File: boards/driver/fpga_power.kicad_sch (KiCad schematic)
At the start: 55 parts, among them J2 Barrel_Jack_Switch, J3 Conn_01x24, J4 Conn_01x24, Q87 IRF7413, U10 74LVC245, U11 74LVC245, U12 ADP151-3.3, U13 LTC4231-1, U14 74HC4514, U15 74LVC2G04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

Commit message: Driver: minor schematic cleanup and populated all of the BOM except for resistors
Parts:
- added H10, H9: MountingHole, MountingHole:MountingHole_2mm, symbol Mechanical:MountingHole
- added TP1, TP2, TP3, TP4: TestPoint, TestPoint:TestPoint_Keystone_5000-5004_Miniature, symbol Connector:TestPoint
- C45, C46, C53, C54, C55, C56, C57: MPN (none) -> CL10B104KB8NNWC; Manufacturer (none) -> Samsung Electro-Mechanics; Package (none) -> 0603; Rating (none) -> 50V; Tolerance (none) -> 10%
- C47, C48: MPN (none) -> CL21B105KAFNNNE; Manufacturer (none) -> Samsung Electro-Mechanics; Package (none) -> 0805; Rating (none) -> 25V; Tolerance (none) -> 10%
- C49, C50: MPN (none) -> CL10B105KA8NNNC; Manufacturer (none) -> Samsung Electro-Mechanics; Package (none) -> 0603; Rating (none) -> 25V; Tolerance (none) -> 10%
- C51: MPN (none) -> CL10B101KB8NFNC; Manufacturer (none) -> Samsung Electro-Mechanics; Package (none) -> 0603; Rating (none) -> 50V; Tolerance (none) -> 10%
- C52: MPN (none) -> CL10B103KC8NNNC; Manufacturer (none) -> Samsung Electro-Mechanics; Package (none) -> 0603
- D155: MPN (none) -> SMLD12BN1WT86; Manufacturer (none) -> Rohm Semiconductor; Package (none) -> 0603
- D156: MPN (none) -> SMLD12E3N1WT86; Manufacturer (none) -> Rohm Semiconductor; Package (none) -> 0603
- D157: MPN (none) -> SJW1151CKS-100-TR; Manufacturer (none) -> Stanley Electric Co; Package (none) -> 0603
- H1, H2, H3, H4, H5, H6, H7, H8: MPN (none) -> -
- J2: MPN (none) -> PJ-002A; Manufacturer (none) -> CUI Devices; Package (none) -> TH
- J3, J4: MPN (none) -> PPPC241LFBN-RC; Manufacturer (none) -> Sullins Connector Solutions; Package (none) -> TH
- Q87: MPN (none) -> IRF7413ZTRPBF; Manufacturer (none) -> Infineon Technologies; Package (none) -> 8-SOIC
- U10, U11: MPN (none) -> SN74LVC245APWT; Manufacturer (none) -> Texas Instruments; Package (none) -> 20-TSSOP
- U12: MPN (none) -> ADP151AUJZ-3.3-R7; Manufacturer (none) -> Analog Devices, Inc; Package (none) -> TSOT-23-5
- U13: MPN (none) -> LTC4231CMS-1#PBF; Manufacturer (none) -> Analog Devices, Inc; Package (none) -> 12-TSSOP
- U14: MPN (none) -> CD74HC4514M96; Manufacturer (none) -> Texas Instruments; Package (none) -> 24-SOIC
- U15, U16, U17, U18: MPN (none) -> SN74LVC2G04DBVT; Manufacturer (none) -> Texas Instruments; Package (none) -> SOT-23-6
- U9: MPN (none) -> TEN 5-1221‎; Manufacturer (none) -> Traco Power; Package (none) -> 24-DIP
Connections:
- net +14V: now also TP4.1
- net GND: now also TP1.1, TP2.1, TP3.1
- net +3V3 renamed +3.3V
- no-connect marks 4 -> 9

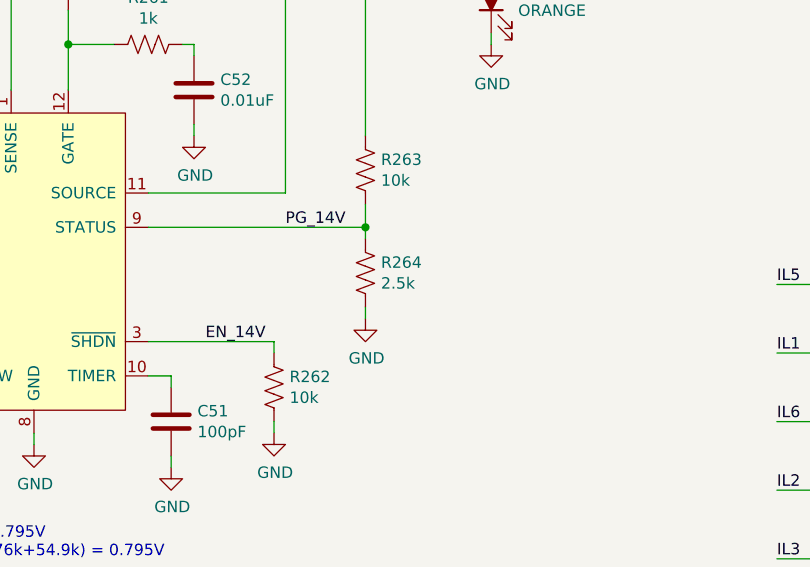
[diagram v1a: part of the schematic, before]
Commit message: Driver: filled out the rest of the BOM, except for defaults for nominal resistances
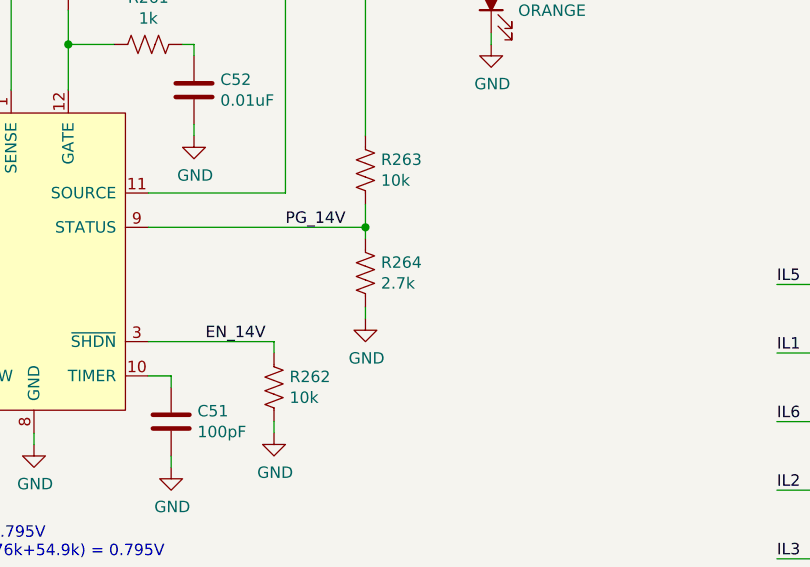
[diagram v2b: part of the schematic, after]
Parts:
- R249, R250: MPN (none) -> RMCF0805ZT0R00; Manufacturer (none) -> Stackpole Electronics Inc; Package (none) -> 0805; Rating (none) -> 1/8W
- R251, R252: MPN (none) -> ERJ-PA3F2001V; Manufacturer (none) -> Panasonic Electronic Components; Package (none) -> 0603; Rating (none) -> 1/3W; Tolerance (none) -> 1%
- R253: MPN (none) -> ERA-3AEB123V; Manufacturer (none) -> Panasonic Electronic Components; Package (none) -> 0603; Rating (none) -> 1/10W; Tolerance (none) -> 0.1%
- R254: MPN (none) -> ERJ-PB3B2401V; Manufacturer (none) -> Panasonic Electronic Components; Package (none) -> 0603; Rating (none) -> 1/5W; Tolerance (none) -> 0.1%
- R255: MPN (none) -> RMCF0603FT1M02; Manufacturer (none) -> Stackpole Electronics Inc; Package (none) -> 0603; Rating (none) -> 1/10W; Tolerance (none) -> 1%
- R256: MPN (none) -> RMCF0603FT2K87; Manufacturer (none) -> Stackpole Electronics Inc; Package (none) -> 0603; Rating (none) -> 1/10W; Tolerance (none) -> 1%
- R257: MPN (none) -> RMCF0603FT9K76; Manufacturer (none) -> Stackpole Electronics Inc; Package (none) -> 0603; Rating (none) -> 1/10W; Tolerance (none) -> 1%
- R258: MPN (none) -> RMCF0603FT54K9; Manufacturer (none) -> Stackpole Electronics Inc; Package (none) -> 0603; Rating (none) -> 1/10W; Tolerance (none) -> 1%
- R259: MPN (none) -> CSR1206FK25L0; Manufacturer (none) -> Stackpole Electronics Inc; Package (none) -> 1206; Rating (none) -> 1/2W; Tolerance (none) -> 1%
- R260: MPN (none) -> ESR03EZPF10R0; Manufacturer (none) -> Rohm Semiconductor; Package (none) -> 0603; Rating (none) -> 1/4W; Tolerance (none) -> 1%
- R261, R265: MPN (none) -> ESR03EZPF1001; Manufacturer (none) -> Rohm Semiconductor; Package (none) -> 0603; Rating (none) -> 1/4W; Tolerance (none) -> 1%
- R262, R263: MPN (none) -> RMCF0603FT10K0; Manufacturer (none) -> Stackpole Electronics Inc; Package (none) -> 0603; Rating (none) -> 1/10W; Tolerance (none) -> 1%
- R264: value 2.5k -> 2.7k; MPN (none) -> RMCF0603JT2K70; Manufacturer (none) -> Stackpole Electronics Inc; Package (none) -> 0603; Rating (none) -> 1/10W; Tolerance (none) -> 1%

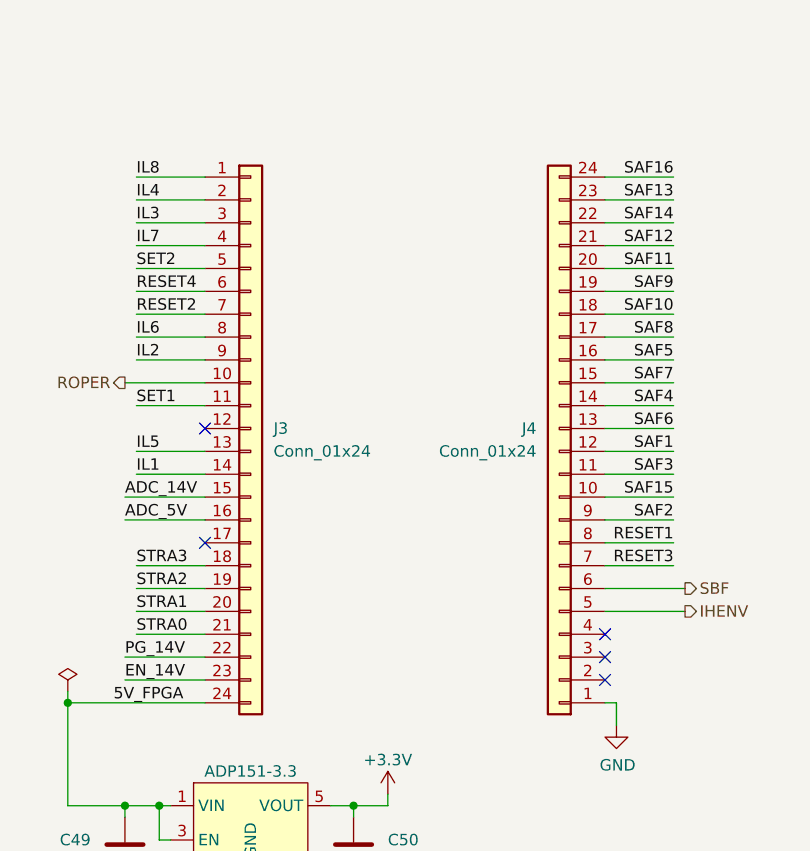
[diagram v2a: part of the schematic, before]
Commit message: Driver: added FPGA ball numbers to the schematic
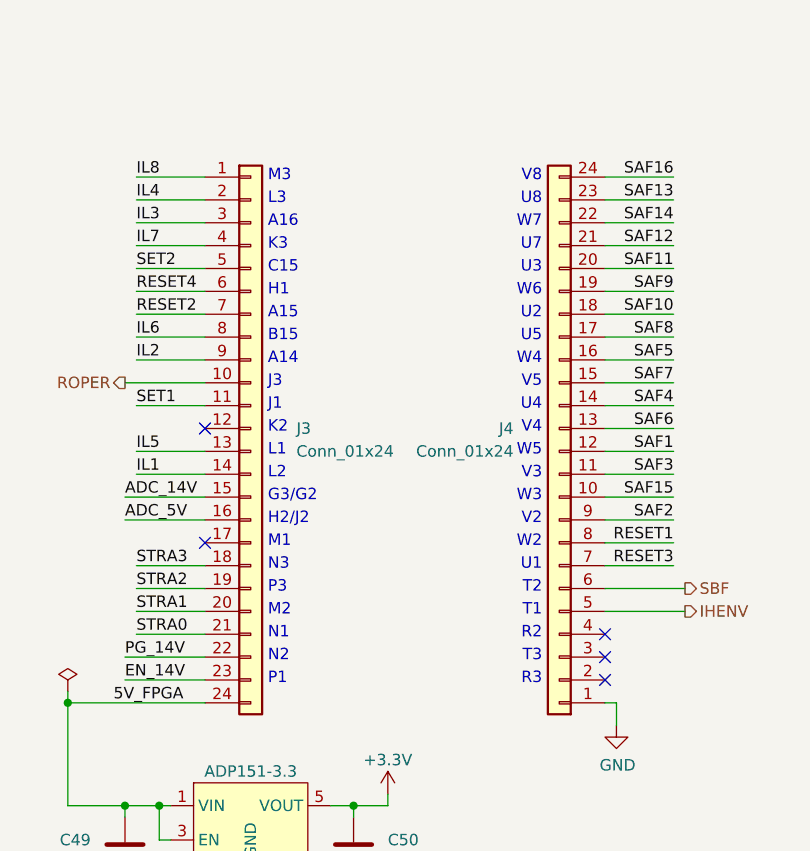
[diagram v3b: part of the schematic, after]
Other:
- note added: "A14"
- note added: "A15"
- note added: "A16"
- note added: "B15"
- note added: "C15"
- note added: "G3/G2"
- note added: "H1"
- note added: "H2/J2"
- note added: "J1"
- note added: "J3"
- note added: "K2"
- note added: "K3"
- note added: "L1"
- note added: "L2"
- note added: "L3"
- note added: "M1"
- note added: "M2"
- note added: "M3"
- note added: "N1"
- note added: "N2"
- note added: "N3"
- note added: "P1"
- note added: "P3"
- note added: "R2"
- note added: "R3"
- note added: "T1"
- note added: "T2"
- note added: "T3"
- note added: "U1"
- note added: "U2"
- note added: "U3"
- note added: "U4"
- note added: "U5"
- note added: "U7"
- note added: "U8"
- note added: "V2"
- note added: "V3"
- note added: "V4"
- note added: "V5"
- note added: "V8"
- note added: "W2"
- note added: "W3"
- note added: "W4"
- note added: "W5"
- note added: "W6"
- note added: "W7"
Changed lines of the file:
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@@
     (stroke (width 0) (type default) (color 0 0 0 0))
+  )
+  (text "K2" (at 159.385 175.895 0)
+    (effects (font (size 1.27 1.27)) (justify left bottom))
+  )
+  (text "N1" (at 159.385 198.755 0)
+    (effects (font (size 1.27 1.27)) (justify left bottom))
+  )
+  (text "W4" (at 189.865 168.275 180)
+    (effects (font (size 1.27 1.27)) (justify right bottom))
+  )
+  (text "G3/G2" (at 159.385 183.515 0)
+    (effects (font (size 1.27 1.27)) (justify left bottom))
+  )
+  (text "L2" (at 159.385 180.975 0)
+    (effects (font (size 1.27 1.27)) (justify left bottom))
+  )
+  (text "A14" (at 159.385 168.275 0)
+    (effects (font (size 1.27 1.27)) (justify left bottom))
+  )
+  (text "C15" (at 159.385 158.115 0)
+    (effects (font (size 1.27 1.27)) (justify left bottom))
+  )
+  (text "L3" (at 159.385 150.495 0)
+    (effects (font (size 1.27 1.27)) (justify left bottom))
+  )
+  (text "V2" (at 189.865 186.055 180)
+    (effects (font (size 1.27 1.27)) (justify right bottom))
+  )
+  (text "H2/J2" (at 159.385 186.055 0)
+    (effects (font (size 1.27 1.27)) (justify left bottom))
+  )
+  (text "R3" (at 189.865 203.835 180)
+    (effects (font (size 1.27 1.27)) (justify right bottom))
+  )
+  (text "U1" (at 189.865 191.135 180)
+    (effects (font (size 1.27 1.27)) (justify right bottom))
+  )
+  (text "P3" (at 159.385 193.675 0)
+    (effects (font (size 1.27 1.27)) (justify left bottom))
+  )
+  (text "N3" (at 159.385 191.135 0)
+    (effects (font (size 1.27 1.27)) (justify left bottom))
+  )
+  (text "J3" (at 159.385 170.815 0)
+    (effects (font (size 1.27 1.27)) (justify left bottom))
+  )
+  (text "U7" (at 189.865 155.575 180)
+    (effects (font (size 1.27 1.27)) (justify right bottom))
+  )
+  (text "W2" (at 189.865 188.595 180)
+    (effects (font (size 1.27 1.27)) (justify right bottom))
+  )
+  (text "U4" (at 189.865 173.355 180)
+    (effects (font (size 1.27 1.27)) (justify right bottom))
+  )
+  (text "T2" (at 189.865 193.675 180)
+    (effects (font (size 1.27 1.27)) (justify right bottom))
+  )
+  (text "V5" (at 189.865 170.815 180)
+    (effects (font (size 1.27 1.27)) (justify right bottom))
+  )
+  (text "A15" (at 159.385 163.195 0)
+    (effects (font (size 1.27 1.27)) (justify left bottom))
+  )
+  (text "H1" (at 159.385 160.655 0)
+    (effects (font (size 1.27 1.27)) (justify left bottom))
+  )
+  (text "N2" (at 159.385 201.295 0)
+    (effects (font (size 1.27 1.27)) (justify left bottom))
+  )
+  (text "M1" (at 159.385 188.595 0)
+    (effects (font (size 1.27 1.27)) (justify left bottom))
+  )
+  (text "M2" (at 159.385 196.215 0)
+    (effects (font (size 1.27 1.27)) (justify left bottom))
+  )
+  (text "W3" (at 189.865 183.515 180)
+    (effects (font (size 1.27 1.27)) (justify right bottom))
+  )
+  (text "R2" (at 189.865 198.755 180)
+    (effects (font (size 1.27 1.27)) (justify right bottom))
+  )
+  (text "T3" (at 189.865 201.295 180)
+    (effects (font (size 1.27 1.27)) (justify right bottom))
+  )
+  (text "W5" (at 189.865 178.435 180)
+    (effects (font (size 1.27 1.27)) (justify right bottom))
+  )
+  (text "K3" (at 159.385 155.575 0)
+    (effects (font (size 1.27 1.27)) (justify left bottom))
+  )
+  (text "V8" (at 189.865 147.955 180)
+    (effects (font (size 1.27 1.27)) (justify right bottom))
+  )
+  (text "M3" (at 159.385 147.955 0)
+    (effects (font (size 1.27 1.27)) (justify left bottom))
+  )
+  (text "J1" (at 159.385 173.355 0)
+    (effects (font (size 1.27 1.27)) (justify left bottom))
   )
   (text "Vov (@ 15.75V) = 15.75*(54.9k/(1020k+2.87k+9.76k+54.9k)) = 0.795V\nVuvl (@ 12.80V) = 12.80*(2.87k+9.76k+54.9k)/(1020k+2.87k+9.76k+54.9k) = 0.795V"
     (at 128.27 114.3 0)
     (effects (font (size 1.27 1.27)) (justify left bottom))
+  )
+  (text "U5" (at 189.865 165.735 180)
+    (effects (font (size 1.27 1.27)) (justify right bottom))
+  )
+  (text "L1" (at 159.385 178.435 0)
+    (effects (font (size 1.27 1.27)) (justify left bottom))
+  )
+  (text "U8" (at 189.865 150.495 180)
+    (effects (font (size 1.27 1.27)) (justify right bottom))
+  )
+  (text "W7" (at 189.865 153.035 180)
+    (effects (font (size 1.27 1.27)) (justify right bottom))
+  )
+  (text "T1" (at 189.865 196.215 180)
+    (effects (font (size 1.27 1.27)) (justify right bottom))
+  )
+  (text "V4" (at 189.865 175.895 180)
+    (effects (font (size 1.27 1.27)) (justify right bottom))
+  )
+  (text "B15" (at 159.385 165.735 0)
+    (effects (font (size 1.27 1.27)) (justify left bottom))
+  )
+  (text "A16" (at 159.385 153.035 0)
+    (effects (font (size 1.27 1.27)) (justify left bottom))
+  )
+  (text "U3" (at 189.865 158.115 180)
+    (effects (font (size 1.27 1.27)) (justify right bottom))
+  )
+  (text "W6" (at 189.865 160.655 180)
+    (effects (font (size 1.27 1.27)) (justify right bottom))
+  )
+  (text "P1" (at 159.385 203.835 0)
+    (effects (font (size 1.27 1.27)) (justify left bottom))
+  )
+  (text "U2" (at 189.865 163.195 180)
+    (effects (font (size 1.27 1.27)) (justify right bottom))
+  )
+  (text "V3" (at 189.865 180.975 180)
+    (effects (font (size 1.27 1.27)) (justify right bottom))
   )
   (label "IL1" (at 144.78 180.34 0)
@@
   (symbol (lib_id "Connector_Generic:Conn_01x24") (at 157.48 175.26 0) (unit 1)
     (in_bom yes) (on_board yes)
-    (property "Reference" "J3" (id 0) (at 160.02 175.26 0)
+    (property "Reference" "J3" (id 0) (at 162.56 175.26 0)
       (effects (font (size 1.27 1.27)) (justify left))
     )
-    (property "Value" "Conn_01x24" (id 1) (at 160.02 177.8 0)
+    (property "Value" "Conn_01x24" (id 1) (at 162.56 177.8 0)
       (effects (font (size 1.27 1.27)) (justify left))
     )
@@
   (symbol (lib_id "Connector_Generic:Conn_01x24") (at 191.77 177.8 180) (unit 1)
     (in_bom yes) (on_board yes)
-    (property "Reference" "J4" (id 0) (at 189.23 175.26 0)
+    (property "Reference" "J4" (id 0) (at 186.69 175.26 0)
       (effects (font (size 1.27 1.27)) (justify left))
     )
-    (property "Value" "Conn_01x24" (id 1) (at 189.23 177.8 0)
+    (property "Value" "Conn_01x24" (id 1) (at 186.69 177.8 0)
       (effects (font (size 1.27 1.27)) (justify left))
     )

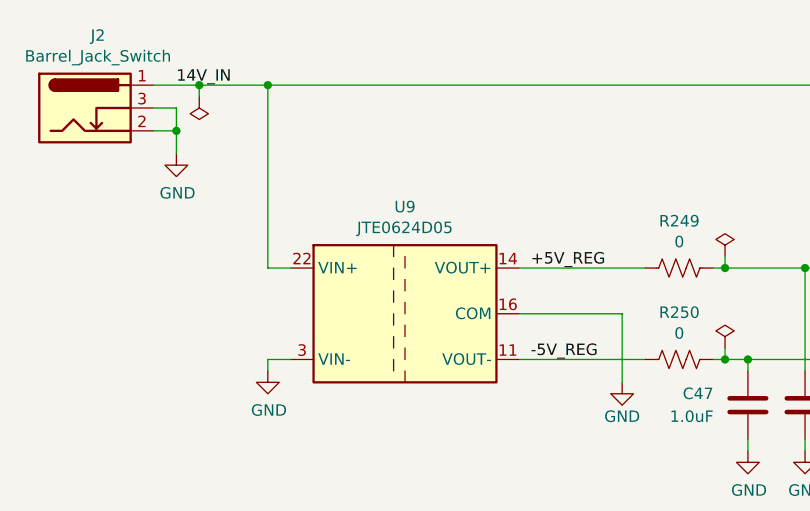
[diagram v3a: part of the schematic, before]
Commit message: Driver: corrected reference divider resistor and added diode direction symbols to the silkscreen
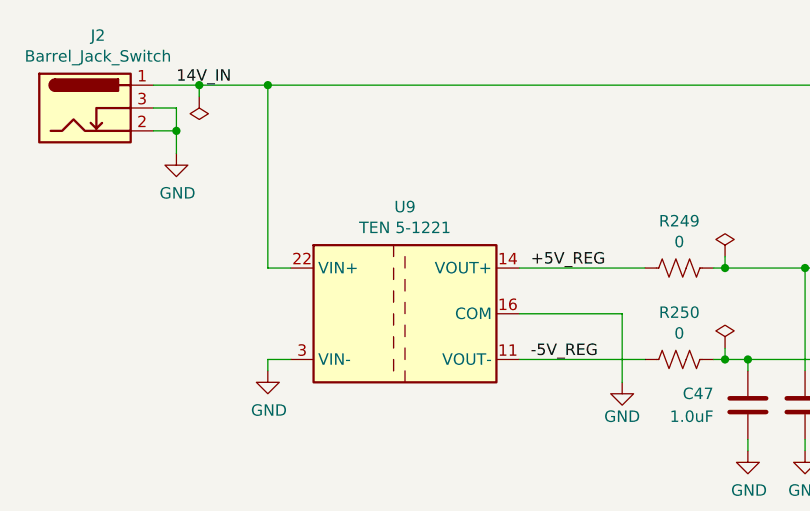
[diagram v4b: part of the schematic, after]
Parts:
- U9: value JTE0624D05 -> TEN 5-1221‎
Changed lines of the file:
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@@
     (in_bom yes) (on_board yes)
     (property "Reference" "U9" (id 0) (at 62.23 50.3682 0))
-    (property "Value" "JTE0624D05" (id 1) (at 62.23 52.6796 0))
+    (property "Value" "TEN 5-1221‎" (id 1) (at 62.23 52.6796 0))
     (property "Footprint" "Converter_DCDC:Converter_DCDC_XP_POWER_JTExxxxDxx_THT" (id 2) (at 62.23 72.39 0)
       (effects (font (size 1.27 1.27) italic) hide)
